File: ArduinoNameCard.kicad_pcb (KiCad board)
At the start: 2 copper layers, 91 x 55 mm, 30 parts, among them J1 Conn_01x05, J2 Conn_01x04, J3 Conn_01x06, J4 Conn_01x08, J5 Conn_01x06, SW1 SW_Push

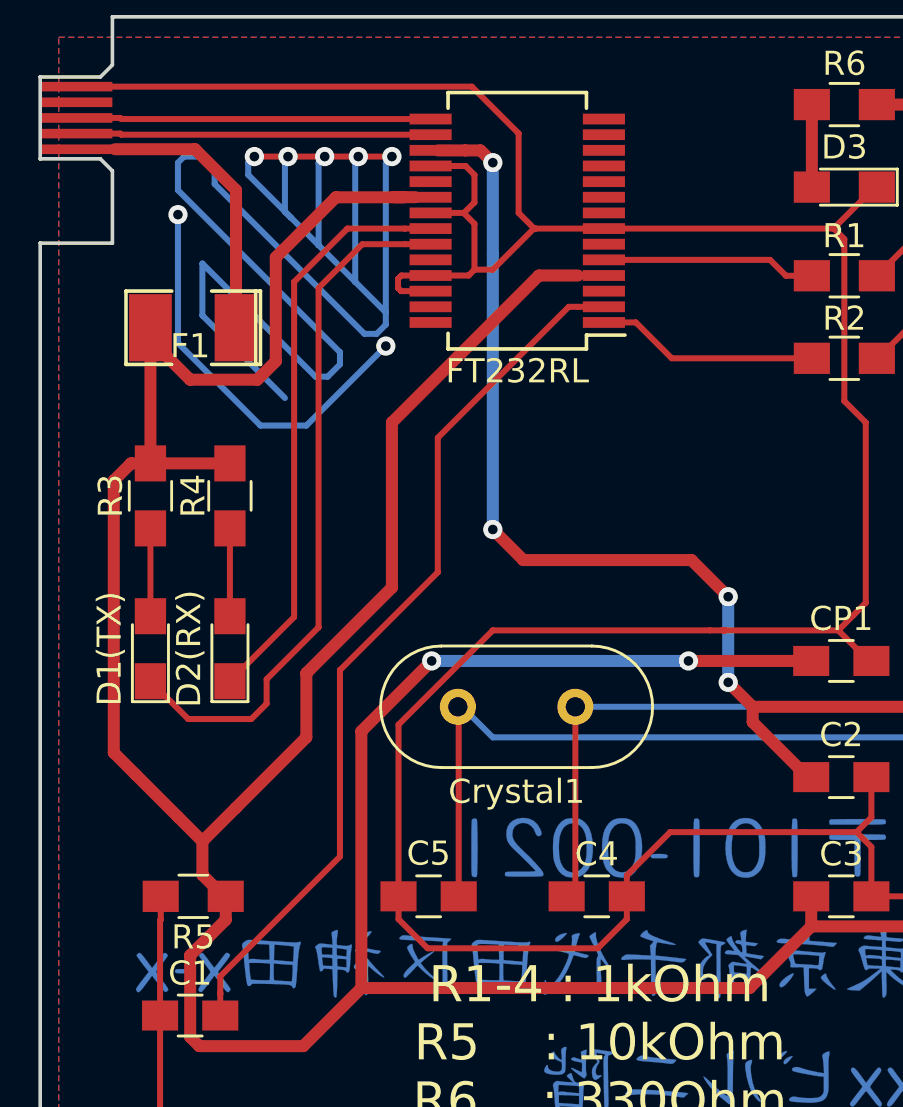
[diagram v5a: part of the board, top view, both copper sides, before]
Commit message: ・DRCで配線幅についてエラーが出ていたので修正した ・R5のシルクの位置を上付きに修正した
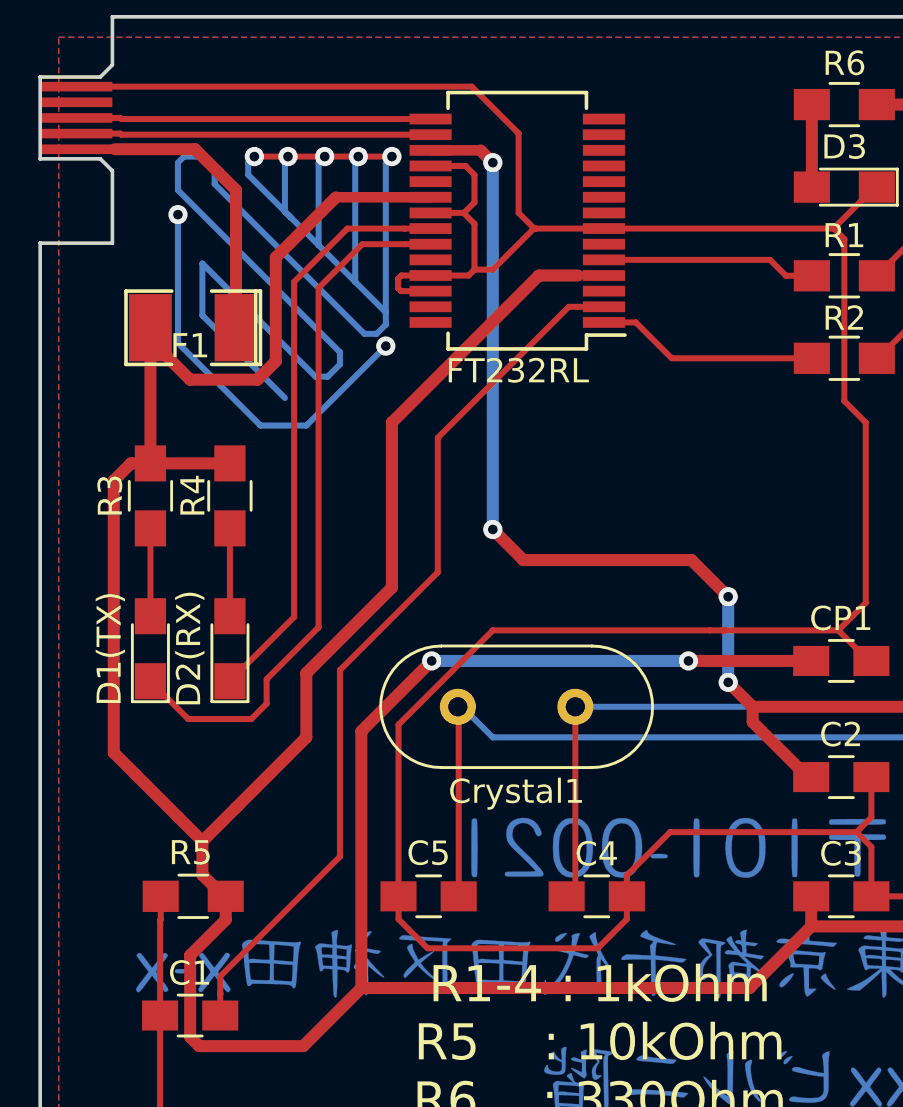
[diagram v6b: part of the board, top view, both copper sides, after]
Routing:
- net 5V: track 214.9 -> 214.0 mm
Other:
- net class Default: trace_width 0.5 -> 0.44
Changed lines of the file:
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@@
     (thickness 1.6)
     (drawings 38)
-    (tracks 431)
+    (tracks 429)
     (zones 0)
     (modules 30)
@@
     (47 F.CrtYd user)
     (48 B.Fab user)
-    (49 F.Fab user)
+    (49 F.Fab user hide)
   )
   (setup
-    (last_trace_width 0.5)
+    (last_trace_width 0.44)
     (trace_clearance 0.2)
     (zone_clearance 0.508)
@@
   (net_class Default "これは標準のネット クラスです。"
     (clearance 0.2)
-    (trace_width 0.5)
+    (trace_width 0.44)
     (via_dia 0.8)
     (via_drill 0.4)
@@
     (tags "resistor 0805")
     (attr smd)
-    (fp_text reference R5 (at 0 -1.7 180) (layer F.SilkS)
+    (fp_text reference R5 (at 0.108 1.798 180) (layer F.SilkS)
       (effects (font (size 1 1) (thickness 0.15)))
     )
-    (fp_text value 10k (at 0 1.75 180) (layer F.Fab)
+    (fp_text value 10k (at 0.108 -1.702 180) (layer F.Fab)
       (effects (font (size 1 1) (thickness 0.15)))
     )
@@
   (segment (start 107.315 73.025) (end 107.315 87.122) (width 0.25) (layer F.Cu) (net 2))
   (segment (start 109.134 71.206) (end 107.315 73.025) (width 0.25) (layer F.Cu) (net 2))
-  (segment (start 113.411 67.31) (end 114.046 67.31) (width 0.5) (layer F.Cu) (net 3))
+  (segment (start 111.97 67.306) (end 114.042 67.306) (width 0.44) (layer F.Cu) (net 3))
   (via (at 114.554 83.058) (size 0.8) (drill 0.4) (layers F.Cu B.Cu) (net 3))
   (segment (start 114.554 71.628) (end 114.554 83.058) (width 0.5) (layer B.Cu) (net 3))
   (segment (start 114.554 67.818) (end 114.554 71.628) (width 0.5) (layer B.Cu) (net 3))
   (via (at 114.554 67.818) (size 0.8) (drill 0.4) (layers F.Cu B.Cu) (net 3))
-  (segment (start 125.349 90.424) (end 124.333 89.408) (width 0.5) (layer F.Cu) (net 3))
+  (segment (start 124.333 89.408) (end 125.349 90.424) (width 0.5) (layer F.Cu) (net 3))
   (via (at 124.333 85.852) (size 0.8) (drill 0.4) (layers F.Cu B.Cu) (net 3))
   (segment (start 124.333 85.852) (end 124.333 89.408) (width 0.5) (layer B.Cu) (net 3))
@@
   (segment (start 115.824 84.328) (end 122.809 84.328) (width 0.5) (layer F.Cu) (net 3))
   (segment (start 114.554 83.058) (end 115.824 84.328) (width 0.5) (layer F.Cu) (net 3))
-  (segment (start 113.411 67.31) (end 112.268 67.31) (width 0.5) (layer F.Cu) (net 3))
   (segment (start 114.046 67.31) (end 114.554 67.818) (width 0.5) (layer F.Cu) (net 3))
+  (segment (start 114.042 67.306) (end 114.046 67.31) (width 0.44) (layer F.Cu) (net 3))
   (segment (start 138.741254 107.880254) (end 147.885254 107.880254) (width 0.5) (layer F.Cu) (net 3))
-  (segment (start 151.638 111.633) (end 151.638 112.903) (width 0.5) (layer F.Cu) (net 3))
-  (segment (start 133.985 90.424) (end 136.779 93.218) (width 0.5) (layer F.Cu) (net 3))
-  (via (at 136.779 93.218) (size 0.8) (drill 0.4) (layers F.Cu B.Cu) (net 3))
-  (segment (start 136.779 93.218) (end 136.779 100.33) (width 0.5) (layer B.Cu) (net 3))
-  (segment (start 136.779 100.33) (end 136.779 105.918) (width 0.5) (layer B.Cu) (net 3))
-  (via (at 136.779 105.918) (size 0.8) (drill 0.4) (layers F.Cu B.Cu) (net 3))
-  (segment (start 136.779 105.918) (end 138.741254 107.880254) (width 0.5) (layer F.Cu) (net 3))
-  (segment (start 125.349 90.424) (end 133.985 90.424) (width 0.5) (layer F.Cu) (net 3))
   (segment (start 151.638 111.633) (end 147.885254 107.880254) (width 0.5) (layer F.Cu) (net 3))
+  (segment (start 125.349 90.424) (end 133.985 90.424) (width 0.5) (layer F.Cu) (net 3))
+  (segment (start 136.779 105.918) (end 138.741254 107.880254) (width 0.5) (layer F.Cu) (net 3))
+  (via (at 136.779 105.918) (size 0.8) (drill 0.4) (layers F.Cu B.Cu) (net 3))
+  (segment (start 136.779 100.33) (end 136.779 105.918) (width 0.5) (layer B.Cu) (net 3))
+  (segment (start 136.779 93.218) (end 136.779 100.33) (width 0.5) (layer B.Cu) (net 3))
+  (via (at 136.779 93.218) (size 0.8) (drill 0.4) (layers F.Cu B.Cu) (net 3))
+  (segment (start 133.985 90.424) (end 136.779 93.218) (width 0.5) (layer F.Cu) (net 3))
+  (segment (start 151.638 111.633) (end 151.638 112.903) (width 0.5) (layer F.Cu) (net 3))
   (segment (start 127.782 93.345) (end 127.635 93.345) (width 0.25) (layer F.Cu) (net 3))
   (segment (start 127.635 93.345) (end 125.349 91.059) (width 0.5) (layer F.Cu) (net 3))
@@
   (segment (start 119.297 71.856) (end 126.0727 71.856) (width 0.25) (layer F.Cu) (net 52))
   (segment (start 127.809 72.517) (end 126.7337 72.517) (width 0.25) (layer F.Cu) (net 52))
+  (segment (start 111.97 69.256) (end 108.036 69.256) (width 0.44) (layer F.Cu) (net 53))
+  (segment (start 101.981 76.835) (end 104.775 76.835) (width 0.5) (layer F.Cu) (net 53))
+  (segment (start 104.775 76.835) (end 105.537 76.073) (width 0.5) (layer F.Cu) (net 53))
+  (segment (start 105.537 76.073) (end 105.537 71.755) (width 0.5) (layer F.Cu) (net 53))
+  (segment (start 105.537 71.755) (end 108.036 69.256) (width 0.5) (layer F.Cu) (net 53))
+  (segment (start 101.981 76.835) (end 100.33 75.184) (width 0.5) (layer F.Cu) (net 53))
   (segment (start 161.703 99.79) (end 161.703 98.484) (width 0.5) (layer F.Cu) (net 53))
-  (segment (start 110.4519 69.2531) (end 111.3409 69.2531) (width 0.5) (layer F.Cu) (net 53))
   (segment (start 100.33 80.311) (end 103.632 80.311) (width 0.5) (layer F.Cu) (net 53) (status 20))
-  (segment (start 110.871 69.256) (end 108.036 69.256) (width 0.5) (layer F.Cu) (net 53))
   (segment (start 102.489 96.012) (end 103.886 94.615) (width 0.5) (layer F.Cu) (net 53))
   (segment (start 103.886 94.615) (end 106.807 91.694) (width 0.5) (layer F.Cu) (net 53))
@@
   (segment (start 100.33 74.676) (end 100.33 80.311) (width 0.5) (layer F.Cu) (net 53))
   (segment (start 100.33 74.676) (end 100.33 75.184) (width 0.25) (layer F.Cu) (net 53))
-  (segment (start 100.33 75.184) (end 101.981 76.835) (width 0.5) (layer F.Cu) (net 53))
-  (segment (start 110.871 69.256) (end 111.97 69.256) (width 0.25) (layer F.Cu) (net 53))
-  (segment (start 105.537 71.755) (end 108.036 69.256) (width 0.5) (layer F.Cu) (net 53))
-  (segment (start 105.537 76.073) (end 105.537 71.755) (width 0.5) (layer F.Cu) (net 53))
-  (segment (start 104.775 76.835) (end 105.537 76.073) (width 0.5) (layer F.Cu) (net 53))
-  (segment (start 101.981 76.835) (end 104.775 76.835) (width 0.5) (layer F.Cu) (net 53))
   (segment (start 163.303 94.996) (end 163.303 94.888) (width 0.5) (layer F.Cu) (net 53))
   (segment (start 163.303 94.888) (end 164.103 94.088) (width 0.5) (layer F.Cu) (net 53))

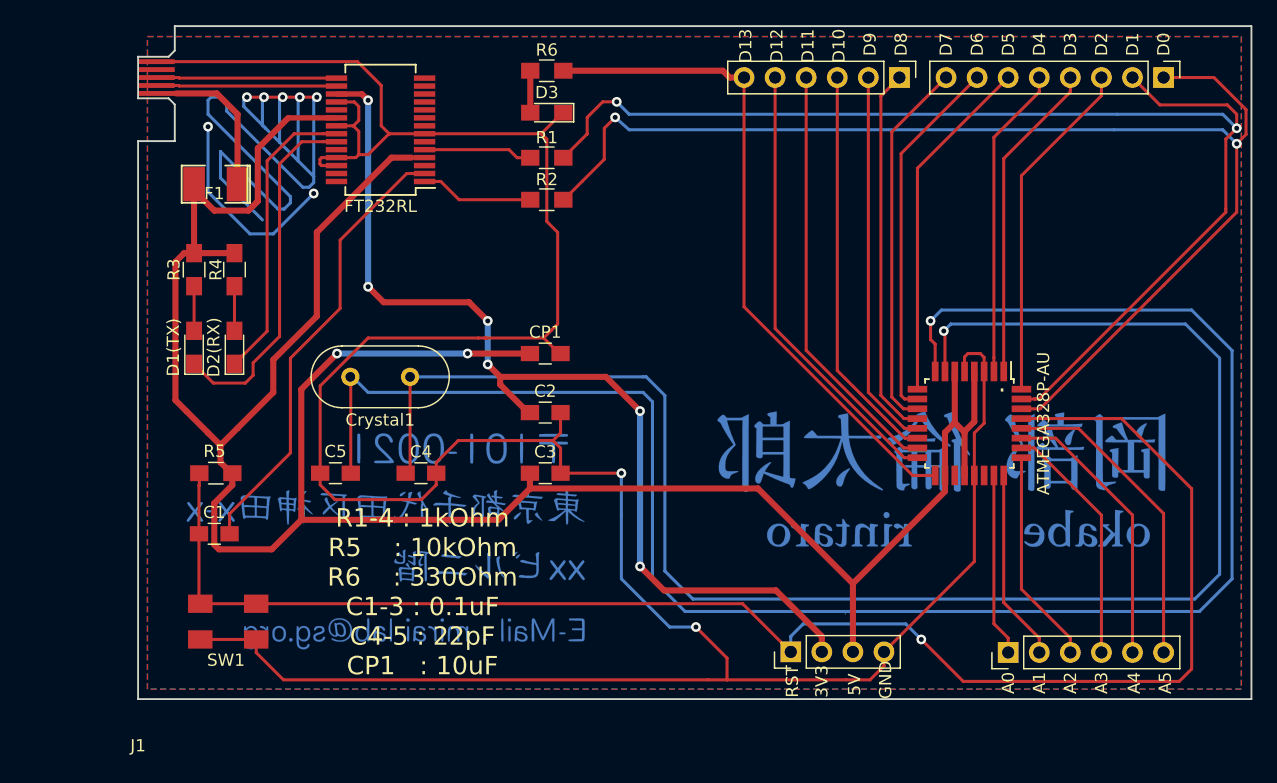
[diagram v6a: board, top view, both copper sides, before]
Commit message: ・READMEに記載している部品を変更した ・端子部分のベタGNDは不要（厚くなる）なので削除した
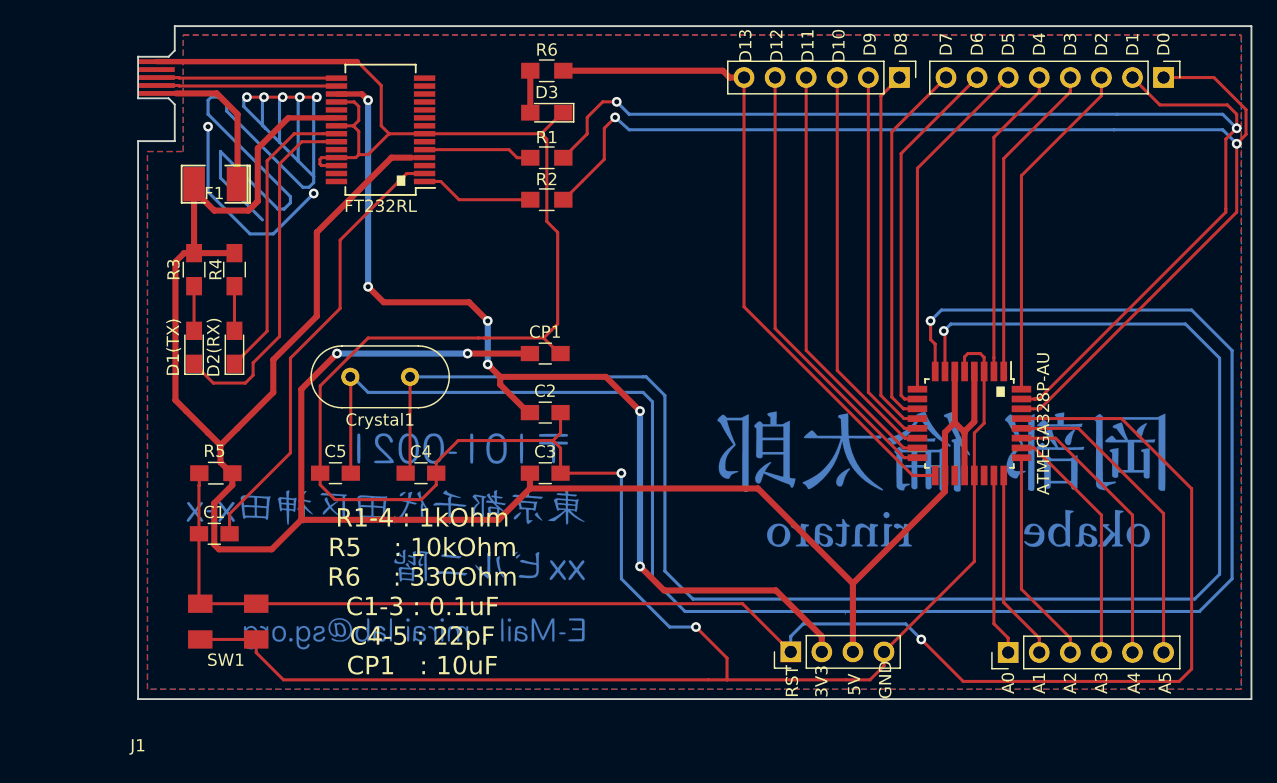
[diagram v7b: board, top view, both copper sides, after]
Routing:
- net +5V: track 13.1 -> 11.4 mm
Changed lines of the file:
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@@
   (general
     (links 74)
-    (no_connects 0)
+    (no_connects 1)
     (area 91.002381 61.21238 187.025001 121.645)
     (thickness 1.6)
-    (drawings 38)
-    (tracks 429)
+    (drawings 39)
+    (tracks 428)
     (zones 0)
     (modules 30)
@@
     )
   )
+  (gr_text . (at 117.25 72.5) (layer F.SilkS)
+    (effects (font (size 5 5) (thickness 0.3)))
+  )
   (gr_text "R1-4 : 1kOhm\nR5    : 10kOhm\nR6    : 330Ohm\nC1-3 : 0.1uF\nC4-5 : 22pF\nCP1   : 10uF" (at 119 108) (layer F.SilkS)
     (effects (font (size 1.5 1.5) (thickness 0.3)))
@@
     (effects (font (size 1 1) (thickness 0.25)))
   )
-  (gr_text . (at 166.37 90.932) (layer F.SilkS)
-    (effects (font (size 1.5 1.5) (thickness 0.3)))
+  (gr_text . (at 166.25 89.75) (layer F.SilkS)
+    (effects (font (size 5 5) (thickness 0.3)))
   )
   (gr_line (start 98.25 64.26) (end 95.75 64.26) (angle 90) (layer Edge.Cuts) (width 0.15))
@@
   (segment (start 128.905 87.249) (end 124.206 87.249) (width 0.25) (layer F.Cu) (net 4))
   (segment (start 124.206 87.249) (end 124.079 87.249) (width 0.25) (layer F.Cu) (net 4))
-  (segment (start 97.25 64.66) (end 113.682 64.66) (width 0.25) (layer F.Cu) (net 4))
+  (segment (start 97.25 64.66) (end 113.682 64.66) (width 0.44) (layer F.Cu) (net 4))
   (segment (start 115.626 66.604) (end 115.626 69.906) (width 0.25) (layer F.Cu) (net 4))
   (segment (start 113.682 64.66) (end 115.626 66.604) (width 0.25) (layer F.Cu) (net 4))
@@
   (segment (start 105.41 108.966) (end 145.161 108.966) (width 0.25) (layer F.Cu) (net 45))
   (segment (start 102.185 67.26) (end 98.856 67.26) (width 0.5) (layer F.Cu) (net 46))
-  (segment (start 97.25 67.26) (end 98.856 67.26) (width 0.25) (layer F.Cu) (net 46))
   (segment (start 103.886 68.961) (end 103.886 74.676) (width 0.5) (layer F.Cu) (net 46))
   (segment (start 102.185 67.26) (end 103.886 68.961) (width 0.5) (layer F.Cu) (net 46))
@@
   (segment (start 127.782 99.548) (end 127.782 98.298) (width 0.5) (layer F.Cu) (net 53))
   (segment (start 127.782 98.298) (end 127.782 99.2483) (width 0.25) (layer F.Cu) (net 53))
-  (zone (net 4) (net_name GND) (layer F.Cu) (hatch edge 0.508)
+  (zone (net 4) (net_name GND) (layer B.Cu) (hatch edge 0.508)
     (connect_pads (clearance 0.508))
     (min_thickness 0.254)
@@
     (polygon
       (pts
-        (xy 185.928 115.951) (xy 96.52 115.951) (xy 96.52 62.611) (xy 185.928 62.611)
+        (xy 185.928 62.611) (xy 185.928 115.951) (xy 96.52 115.951) (xy 96.52 72.009) (xy 99.441 72.009)
+        (xy 99.441 62.484) (xy 185.928 62.484)
       )
     )
   )
-  (zone (net 4) (net_name GND) (layer B.Cu) (hatch edge 0.508)
+  (zone (net 4) (net_name GND) (layer F.Cu) (hatch edge 0.508)
     (connect_pads (clearance 0.508))
     (min_thickness 0.254)
@@
     (polygon
       (pts
-        (xy 185.928 115.951) (xy 96.52 115.951) (xy 96.52 62.611) (xy 185.928 62.611)
+        (xy 185.928 115.951) (xy 96.52 115.951) (xy 96.52 72.009) (xy 99.441 72.009) (xy 99.441 62.484)
+        (xy 185.928 62.484)
       )
     )

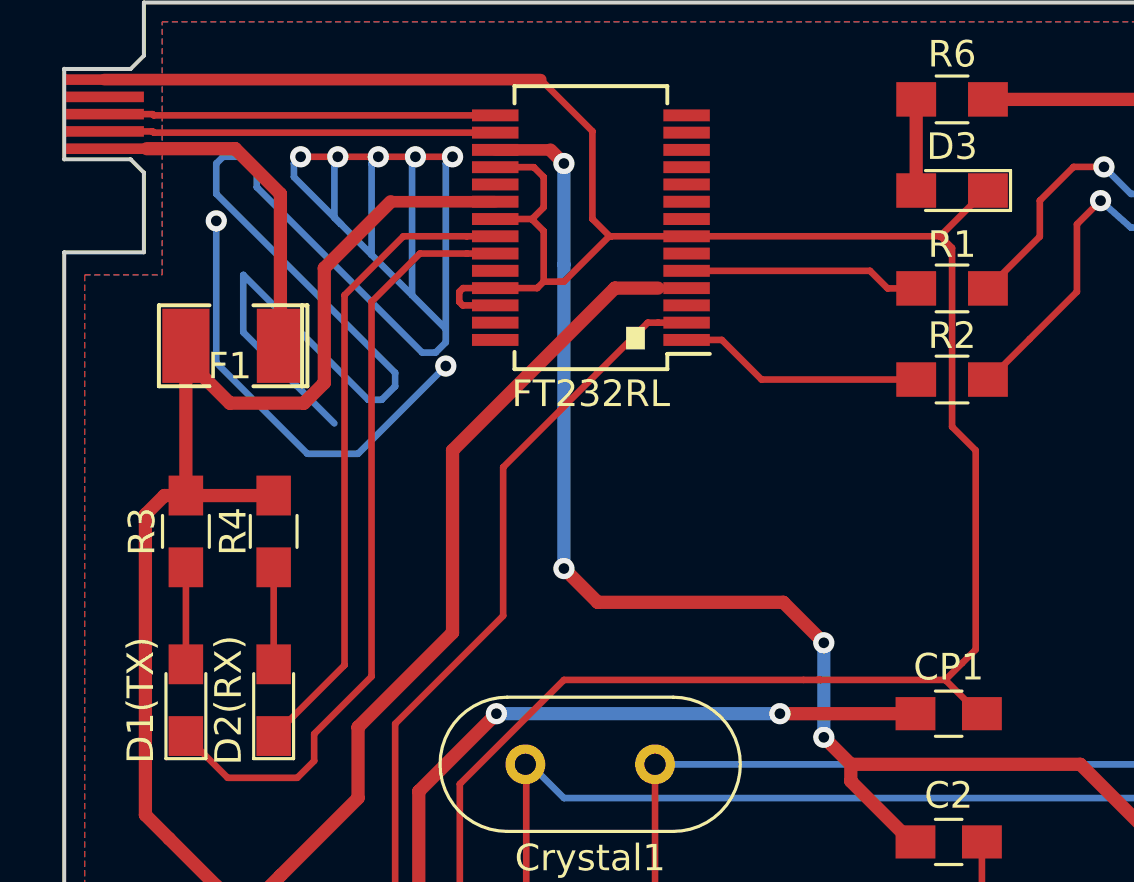
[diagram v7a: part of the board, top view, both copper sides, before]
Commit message: LEDに向きのシルクを追加
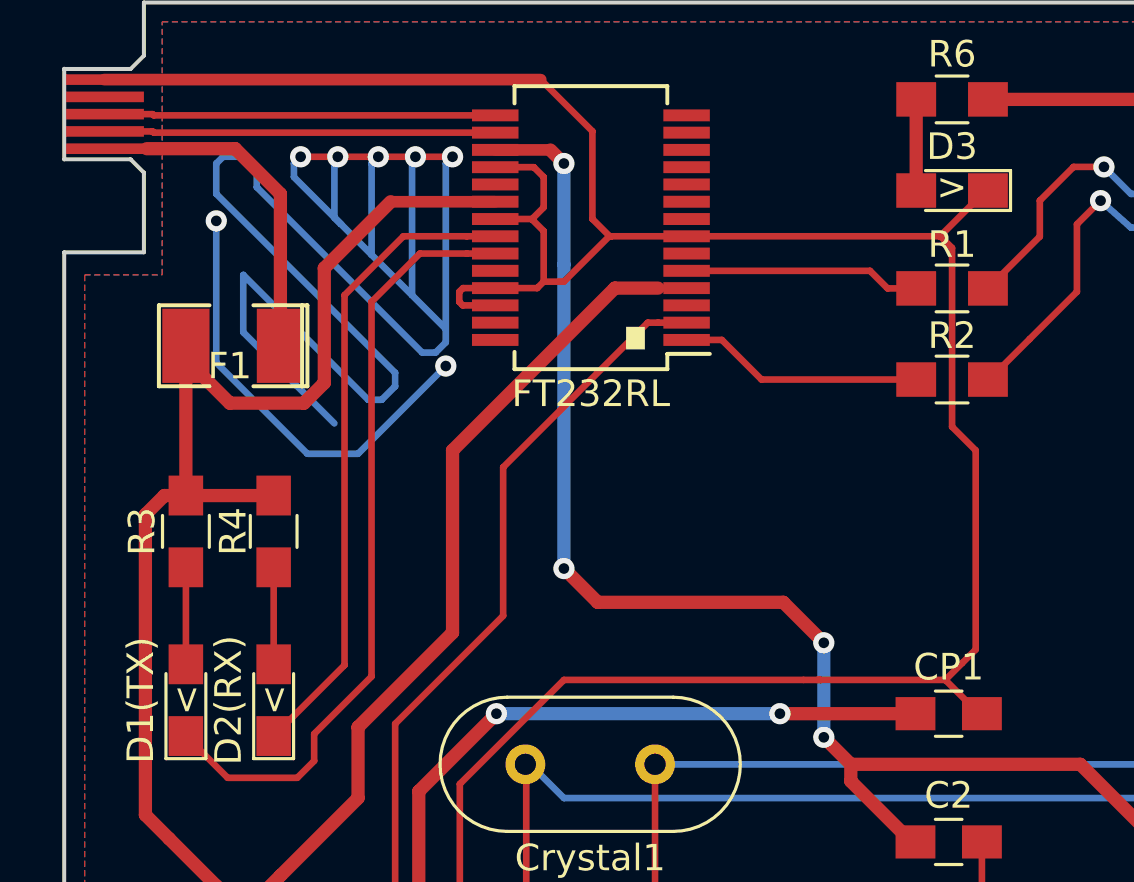
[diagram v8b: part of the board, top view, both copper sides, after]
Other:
- board text added: ">"
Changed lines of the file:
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@@
     (area 91.002381 61.21238 187.025001 121.645)
     (thickness 1.6)
-    (drawings 39)
+    (drawings 42)
     (tracks 428)
     (zones 0)
@@
     )
   )
+  (gr_text > (at 100.4 88 270) (layer F.SilkS)
+    (effects (font (size 1 1) (thickness 0.25)))
+  )
+  (gr_text > (at 129.15 68.7) (layer F.SilkS)
+    (effects (font (size 1 1) (thickness 0.25)))
+  )
+  (gr_text > (at 103.7 88 270) (layer F.SilkS)
+    (effects (font (size 1 1) (thickness 0.25)))
+  )
   (gr_text . (at 117.25 72.5) (layer F.SilkS)
